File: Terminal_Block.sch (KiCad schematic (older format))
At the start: 0 parts

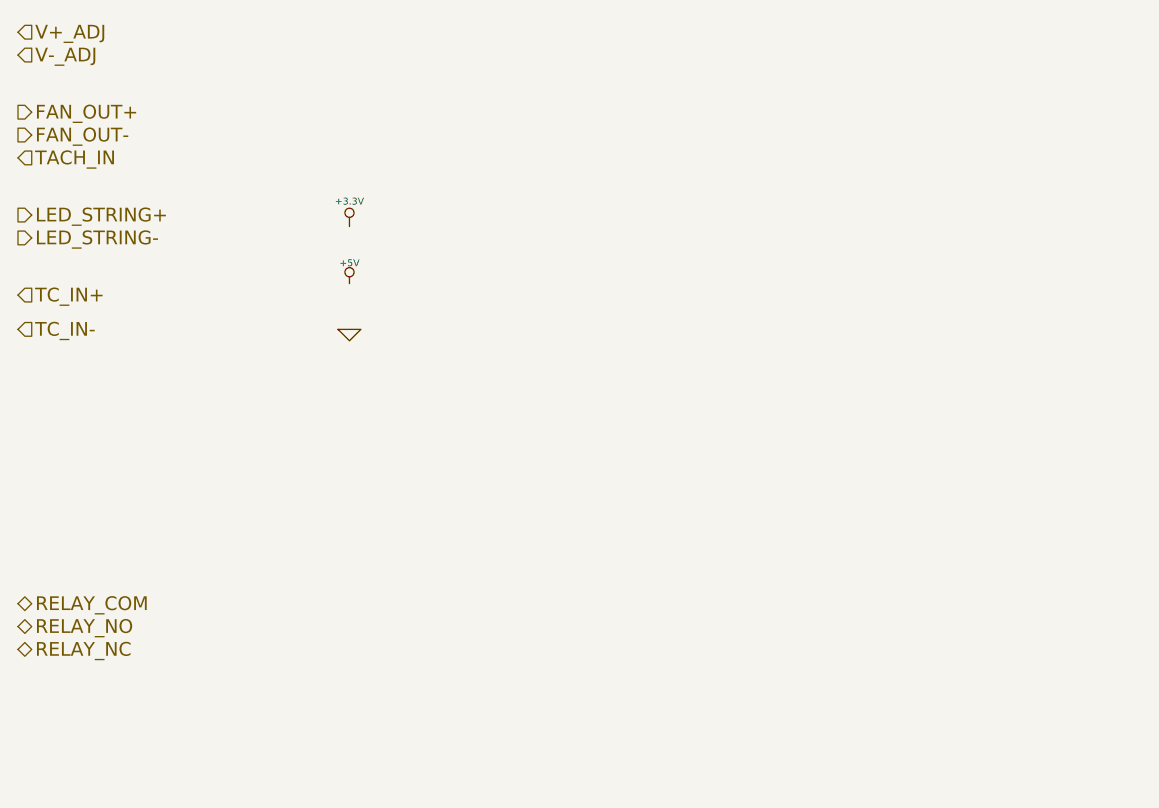
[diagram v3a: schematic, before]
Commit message: Initial layout of Arduino and Fan-Current
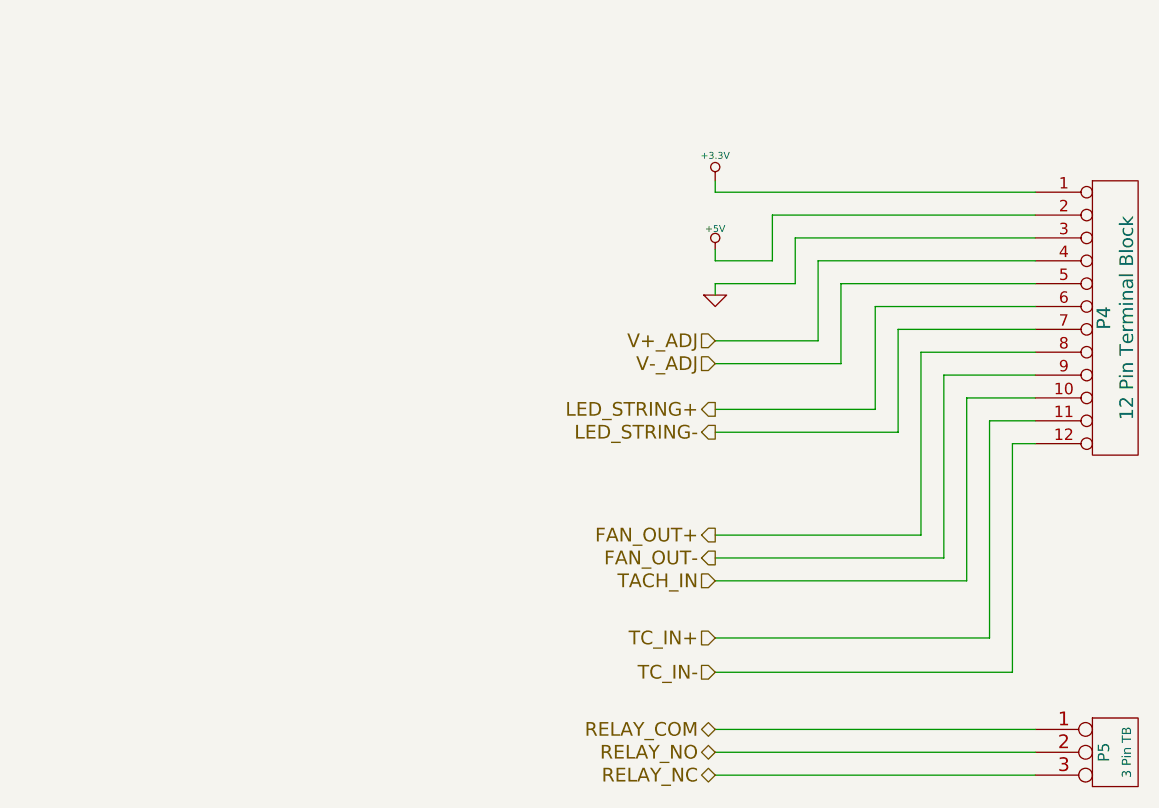
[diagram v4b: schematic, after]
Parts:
- added P4: 12 Pin Terminal Block, symbol CONN_12
- added P5: 3 Pin TB, symbol CONN_3
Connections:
- net +3.3V: now also P4.1 (P1)
- net +5V: now also P4.2 (P2)
- net FAN_OUT+: now also P4.8 (P8)
- net FAN_OUT-: now also P4.9 (P9)
- net GND: now also P4.3 (P3)
- net LED_STRING+: now also P4.6 (P6)
- net LED_STRING-: now also P4.7 (P7)
- net RELAY_COM: now also P5.1 (P1)
- net RELAY_NC: now also P5.3 (P3)
- net RELAY_NO: now also P5.2 (PM)
- net TACH_IN: now also P4.10 (P10)
- net TC_IN+: now also P4.11 (P11)
- net TC_IN-: now also P4.12 (P12)
- net V+_ADJ: now also P4.4 (P4)
- net V-_ADJ: now also P4.5 (P5)
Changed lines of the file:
@@
 Sheet 8 9
 Title ""
-Date "21 feb 2014"
+Date "22 feb 2014"
 Rev ""
 Comp ""
@@
 Comment4 ""
 $EndDescr
-Text HLabel 1850 2000 2    60   Input ~ 0
+Text HLabel 4900 3350 0    60   Input ~ 0
 V+_ADJ
-Text HLabel 1850 2100 2    60   Input ~ 0
+Text HLabel 4900 3450 0    60   Input ~ 0
 V-_ADJ
-Text HLabel 1850 2350 2    60   Output ~ 0
+Text HLabel 4900 4200 0    60   Output ~ 0
 FAN_OUT+
-Text HLabel 1850 2450 2    60   Output ~ 0
+Text HLabel 4900 4300 0    60   Output ~ 0
 FAN_OUT-
-Text HLabel 1850 2550 2    60   Input ~ 0
+Text HLabel 4900 4400 0    60   Input ~ 0
 TACH_IN
-Text HLabel 1850 2800 2    60   Output ~ 0
+Text HLabel 4900 3650 0    60   Output ~ 0
 LED_STRING+
-Text HLabel 1850 2900 2    60   Output ~ 0
+Text HLabel 4900 3750 0    60   Output ~ 0
 LED_STRING-
-Text HLabel 1850 3150 2    60   Input ~ 0
+Text HLabel 4900 4650 0    60   Input ~ 0
 TC_IN+
-Text HLabel 1850 3300 2    60   Input ~ 0
+Text HLabel 4900 4800 0    60   Input ~ 0
 TC_IN-
-Text HLabel 1850 4500 2    60   BiDi ~ 0
+Text HLabel 4900 5050 0    60   BiDi ~ 0
 RELAY_COM
-Text HLabel 1850 4600 2    60   BiDi ~ 0
+Text HLabel 4900 5150 0    60   BiDi ~ 0
 RELAY_NO
-Text HLabel 1850 4700 2    60   BiDi ~ 0
+Text HLabel 4900 5250 0    60   BiDi ~ 0
 RELAY_NC
 $Comp
-L +3.3V #PWR053
+L +3.3V #PWR048
 U 1 1 52F45F58
-P 3300 2850
-F 0 "#PWR053" H 3300 2810 30  0001 C CNN
-F 1 "+3.3V" H 3300 2960 30  0000 C CNN
-F 2 "" H 3300 2850 60  0000 C CNN
-F 3 "" H 3300 2850 60  0000 C CNN
-	1    3300 2850
+P 4900 2650
+F 0 "#PWR048" H 4900 2610 30  0001 C CNN
+F 1 "+3.3V" H 4900 2760 30  0000 C CNN
+F 2 "" H 4900 2650 60  0000 C CNN
+F 3 "" H 4900 2650 60  0000 C CNN
+	1    4900 2650
 	1    0    0    -1
 $EndComp
 $Comp
-L +5V #PWR054
+L +5V #PWR049
 U 1 1 52F45F67
-P 3300 3100
-F 0 "#PWR054" H 3300 3190 20  0001 C CNN
-F 1 "+5V" H 3300 3190 30  0000 C CNN
-F 2 "" H 3300 3100 60  0000 C CNN
-F 3 "" H 3300 3100 60  0000 C CNN
-	1    3300 3100
+P 4900 2950
+F 0 "#PWR049" H 4900 3040 20  0001 C CNN
+F 1 "+5V" H 4900 3040 30  0000 C CNN
+F 2 "" H 4900 2950 60  0000 C CNN
+F 3 "" H 4900 2950 60  0000 C CNN
+	1    4900 2950
 	1    0    0    -1
 $EndComp
 $Comp
-L GND #PWR055
+L GND #PWR050
 U 1 1 52F45F76
-P 3300 3300
-F 0 "#PWR055" H 3300 3300 30  0001 C CNN
-F 1 "GND" H 3300 3230 30  0001 C CNN
-F 2 "" H 3300 3300 60  0000 C CNN
-F 3 "" H 3300 3300 60  0000 C CNN
-	1    3300 3300
+P 4900 3150
+F 0 "#PWR050" H 4900 3150 30  0001 C CNN
+F 1 "GND" H 4900 3080 30  0001 C CNN
+F 2 "" H 4900 3150 60  0000 C CNN
+F 3 "" H 4900 3150 60  0000 C CNN
+	1    4900 3150
 	1    0    0    -1
 $EndComp
+$Comp
+L CONN_12 P4
+U 1 1 5307C570
+P 6650 3250
+F 0 "P4" V 6600 3250 60  0000 C CNN
+F 1 "12 Pin Terminal Block" V 6700 3250 60  0000 C CNN
+F 2 "" H 6650 3250 60  0000 C CNN
+F 3 "" H 6650 3250 60  0000 C CNN
+F 4 "On Shore Tech" H 6650 3250 60  0001 C CNN "MFG Name"
+F 5 "OSTTE120104" H 6650 3250 60  0001 C CNN "MFG Part Num"
+F 6 "ED2737" H 6650 3250 60  0001 C CNN "Distrib Part Num 1"
+	1    6650 3250
+	1    0    0    -1
+$EndComp
+Wire Wire Line
+	4900 2700 6300 2700
+Wire Wire Line
+	6300 2800 5150 2800
+Wire Wire Line
+	5150 2800 5150 3000
+Wire Wire Line
+	5150 3000 4900 3000
+Wire Wire Line
+	4900 3000 4900 2950
+Wire Wire Line
+	4900 3150 4900 3100
+Wire Wire Line
+	4900 3100 5250 3100
+Wire Wire Line
+	5250 3100 5250 2900
+Wire Wire Line
+	5250 2900 6300 2900
+Wire Wire Line
+	4900 3350 5350 3350
+Wire Wire Line
+	5350 3350 5350 3000
+Wire Wire Line
+	5350 3000 6300 3000
+Wire Wire Line
+	6300 3100 5450 3100
+Wire Wire Line
+	5450 3100 5450 3450
+Wire Wire Line
+	5450 3450 4900 3450
+Wire Wire Line
+	4900 3650 5600 3650
+Wire Wire Line
+	5600 3650 5600 3200
+Wire Wire Line
+	5600 3200 6300 3200
+Wire Wire Line
+	6300 3300 5700 3300
+Wire Wire Line
+	5700 3300 5700 3750
+Wire Wire Line
+	5700 3750 4900 3750
+Wire Wire Line
+	4900 4200 5800 4200
+Wire Wire Line
+	5800 4200 5800 3400
+Wire Wire Line
+	5800 3400 6300 3400
+Wire Wire Line
+	6300 3500 5900 3500
+Wire Wire Line
+	5900 3500 5900 4300
+Wire Wire Line
+	5900 4300 4900 4300
+Wire Wire Line
+	4900 4400 6000 4400
+Wire Wire Line
+	6000 4400 6000 3600
+Wire Wire Line
+	6000 3600 6300 3600
+Wire Wire Line
+	6300 3700 6100 3700
+Wire Wire Line
+	6100 3700 6100 4650
+Wire Wire Line
+	6100 4650 4900 4650
+Wire Wire Line
+	4900 4800 6200 4800
+Wire Wire Line
+	6200 4800 6200 3800
+Wire Wire Line
+	6200 3800 6300 3800
+Wire Wire Line
+	4900 2650 4900 2700
+$Comp
+L CONN_3 P5
+U 1 1 5307C76F
+P 6650 5150
+F 0 "P5" V 6600 5150 50  0000 C CNN
+F 1 "3 Pin TB" V 6700 5150 40  0000 C CNN
+F 2 "" H 6650 5150 60  0000 C CNN
+F 3 "" H 6650 5150 60  0000 C CNN
+F 4 "Phoenix Contact" H 6650 5150 60  0001 C CNN "MFG Name"
+F 5 "1935174" H 6650 5150 60  0001 C CNN "MFG Part Num"
+F 6 "277-1578" H 6650 5150 60  0001 C CNN "Distrib Part Num 1"
+	1    6650 5150
+	1    0    0    -1
+$EndComp
+Wire Wire Line
+	6300 5050 4900 5050
+Wire Wire Line
+	4900 5150 6300 5150
+Wire Wire Line
+	6300 5250 4900 5250
 $EndSCHEMATC
